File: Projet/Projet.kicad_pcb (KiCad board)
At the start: 4 copper layers, 111 x 81 mm, 67 parts, among them J201 Conn_02x07_Odd_Even, J301 Moteur 1, J302 Moteur 1, J303 Conn_01x03, J401 optiqueGauche, J402 couleursDroit, J403 couleursGauche, J404 optiqueDroit, J405 tofGauche, J406 tofDroit, J501 alim batterie, J502 Conn_01x03_Female, SW201 SW_MEC_5E, U201 STM32G070RBT6, U301 ZXBM5210-S, U302 ZXBM5210-S, U501 AZ1117-5.0, U502 MIC5317-3.3, Y201 16 MHz

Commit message: Routing
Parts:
- removed SW201: SW_MEC_5E, Button_Switch_SMD:SW_SPST_EVQQ2
- added C307: 1uF, Capacitor_SMD:C_0603_1608Metric_Pad1.08x0.95mm_HandSolder, F.Cu at (140.5, 124.2)
- added C308: 1uF, Capacitor_SMD:C_0603_1608Metric_Pad1.08x0.95mm_HandSolder, F.Cu at (181.1, 147.3)
- added C309: 1uF, Capacitor_SMD:C_0603_1608Metric_Pad1.08x0.95mm_HandSolder, F.Cu at (138.1, 140.3)
- added C310: 1uF, Capacitor_SMD:C_0603_1608Metric_Pad1.08x0.95mm_HandSolder, F.Cu at (159.7, 147.5)
- added JP304: SolderJumper_2_Open, Jumper:SolderJumper-2_P1.3mm_Open_TrianglePad1.0x1.5mm, F.Cu at (183.3, 126.1)
- added R401: 2.2k, Resistor_SMD:R_0603_1608Metric_Pad0.98x0.95mm_HandSolder, F.Cu at (176.4, 105.5)
- added R402: 2.2k, Resistor_SMD:R_0603_1608Metric_Pad0.98x0.95mm_HandSolder, F.Cu at (181.0, 105.4)
- added R403: 2.2k, Resistor_SMD:R_0603_1608Metric_Pad0.98x0.95mm_HandSolder, F.Cu at (119.9, 106.9)
- added R404: 2.2k, Resistor_SMD:R_0603_1608Metric_Pad0.98x0.95mm_HandSolder, F.Cu at (123.0, 106.9)
- added S201: 2-1437565-7, 2-1437565-7 (1):SW_2-1437565-7, F.Cu at (197.5, 111.5)
- C305, C306: value 100nF -> 10uF
- C502: value 10uF -> 22uF
- J201: footprint Connector_PinHeader_1.00mm:PinHeader_2x07_P1.00mm_Vertical -> Connector_PinHeader_1.27mm:PinHeader_2x07_P1.27mm_Vertical_SMD
- R201, R202: value 60R -> 1k
- R502: value 100k -> 200k
- R503: value 90k -> 100k
- moved H102 107.7 mm to (100.0, 140.0)
- moved H104 107.7 mm to (200.0, 100.0)
- moved D201 101.8 mm to (200.3, 118.6)
- moved R201 101.6 mm to (200.2, 121.4)
- moved J404 92.8 mm to (109.8, 147.4)
- moved C402 82.1 mm to (115.4, 145.8)
- moved C305 67.7 mm to (126.6, 134.5)
- moved JP302 66.2 mm to (132.3, 136.9), turned to 180 degrees
- moved A601 61.9 mm to (207.6, 105.0), turned to 0 degrees
- moved C303 60.7 mm to (141.1, 140.3)
- moved U301 59.7 mm to (140.0, 132.3), turned to 90 degrees
- moved JP303 59.4 mm to (132.3, 132.7), turned to 180 degrees
- moved J301 56.1 mm to (152.1, 147.4), turned to 180 degrees
- moved J405 53.8 mm to (187.3, 100.4)
- moved JP208 52.0 mm to (146.4, 140.4), turned to -90 degrees
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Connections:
- C201 pad 1: STLINK_NRST -> Net-(C201-Pad1)
- C306 pad 1: V+_batterie -> Net-(C306-Pad1)
- J402 pad 1: +3.3V -> +5V
- JP301 pad 2: +3.3V -> +5V
- JP302 pad 2: +3.3V -> +5V
- U201 pad 12: STLINK_NRST -> Net-(C201-Pad1)
- U201 pad 58: BAT_LED -> unconnected-(U201-Pad58)
- U201 pad 7: unconnected-(U201-Pad7) -> +3.3V
- U302 pad 2: V+_batterie -> Net-(C306-Pad1)
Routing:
- net +5V: track 0.00 -> 165.7 mm, vias 0 -> 6
- net V+_batterie: track 0.00 -> 159.7 mm, vias 0 -> 4
- net /Communication/ESP_EN: track 0.00 -> 91.8 mm, vias 0 -> 2
- net /STM32F070RB/OPTQ1: track 0.00 -> 90.2 mm, vias 0 -> 2
- net /STM32F070RB/OPTQ2: track 0.00 -> 66.6 mm, vias 0 -> 2
- net Net-(A601-Pad14): track 0.00 -> 63.8 mm, vias 0 -> 1
- net Net-(C201-Pad1): track 0.00 -> 62.8 mm, vias 0 -> 2
- net Net-(A601-Pad15): track 0.00 -> 58.8 mm, vias 0 -> 2
- net /Driver_Motor_SERVO/SERV_DATA: track 0.00 -> 51.7 mm, vias 0 -> 2
- net /STM32F070RB/TOF1_GPIO1: track 0.00 -> 49.9 mm
- net Net-(JP208-Pad1): track 0.00 -> 49.8 mm, vias 0 -> 2
- net /STM32F070RB/TOF2_SDA: track 0.00 -> 49.6 mm, vias 0 -> 2
- net /STM32F070RB/TOF1_XSHUT: track 0.00 -> 49.3 mm
- net /STM32F070RB/TOF1_SCL: track 0.00 -> 48.9 mm
- net Net-(JP207-Pad1): track 0.00 -> 47.7 mm, vias 0 -> 2
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- added copper zone on In2.Cu, net +3.3V
- added copper zone on B.Cu, net GND
- added copper zone on F.Cu, net GND
- added copper zone on In1.Cu, net GND
- removed copper zone on B.Cu, net (none)
- removed copper zone on F.Cu, net (none)
- removed copper zone on In1.Cu, net (none)
- removed copper zone on In2.Cu, net (none)
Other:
- board size 111 x 81 mm -> 137.1 x 57 mm

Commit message: PCB_ROUTAGE
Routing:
- net /STM32F070RB/TOF2_XSHUT: track 41.7 -> 38.7 mm
- net /STM32F070RB/TOF2_GPIO1: track 37.7 -> 35.6 mm
- net /STM32F070RB/TOF2_SDA: track 49.6 -> 48.1 mm
- net /STM32F070RB/TOF2_SCL: track 44.4 -> 43.0 mm
- net /STM32F070RB/TOF1_SCL: track 48.9 -> 47.7 mm
- net Net-(JP202-Pad2): track 39.7 -> 40.6 mm
- net Net-(JP204-Pad2): track 22.5 -> 21.6 mm
- net Net-(C304-Pad1): track 40.7 -> 39.9 mm
- net Net-(JP201-Pad2): track 32.8 -> 33.3 mm

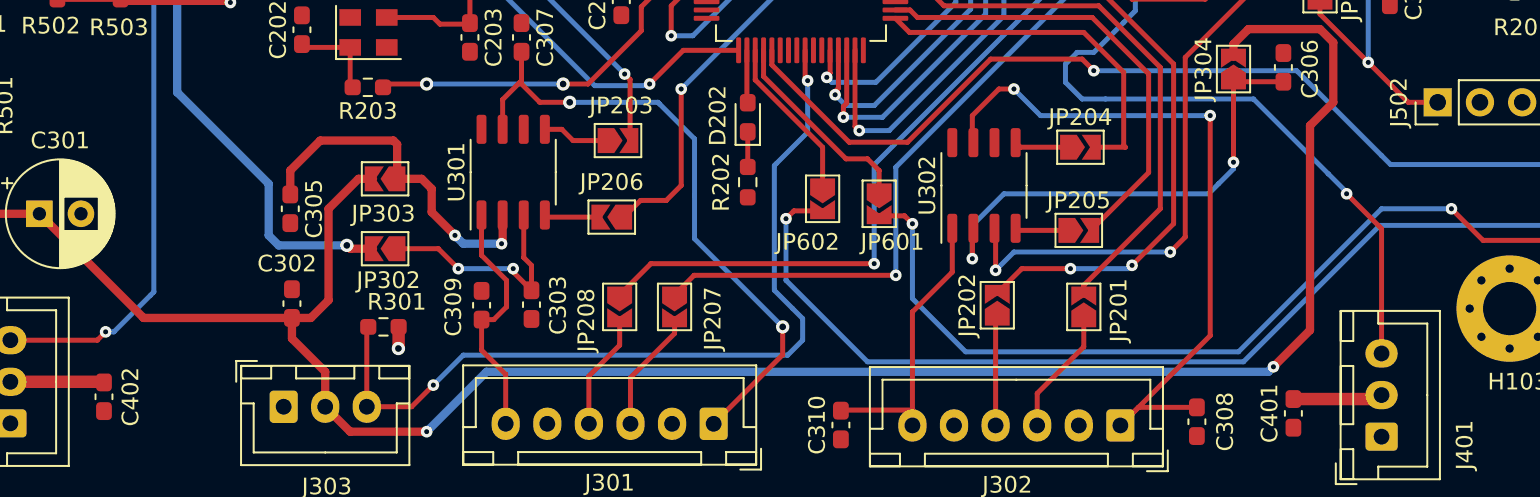
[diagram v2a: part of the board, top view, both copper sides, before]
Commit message: PCB_ROUTAGE_Modif
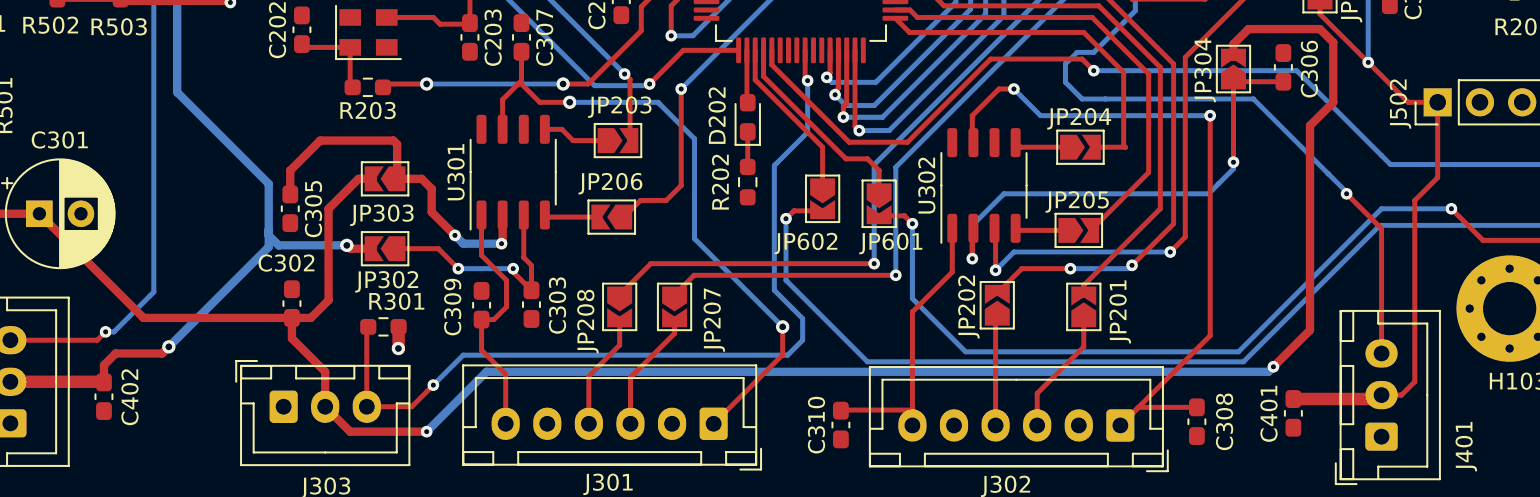
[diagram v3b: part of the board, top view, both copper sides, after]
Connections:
- C401 pad 2: +3.3V -> +5V
- C402 pad 2: +3.3V -> +5V
- J401 pad 2: +3.3V -> +5V
- J404 pad 2: +3.3V -> +5V
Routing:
- net +5V: track 165.7 -> 211.3 mm, vias 6 -> 7
- net +3.3V: track 35.4 -> 24.4 mm
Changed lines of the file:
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@@
       (net 123 "GND") (pintype "passive"))
     (pad "2" smd roundrect (at 0.8625 0 90) (size 1.075 0.95) (layers "F.Cu" "F.Paste" "F.Mask") (roundrect_rratio 0.25)
-      (net 122 "+3.3V") (pintype "passive"))
+      (net 124 "+5V") (pintype "passive"))
     (model "${KICAD6_3DMODEL_DIR}/Capacitor_SMD.3dshapes/C_0603_1608Metric.wrl"
       (offset (xyz 0 0 0))
@@
       (net 123 "GND") (pintype "passive"))
     (pad "2" smd roundrect (at 0.8625 0 90) (size 1.075 0.95) (layers "F.Cu" "F.Paste" "F.Mask") (roundrect_rratio 0.25)
-      (net 122 "+3.3V") (pintype "passive"))
+      (net 124 "+5V") (pintype "passive"))
     (model "${KICAD6_3DMODEL_DIR}/Capacitor_SMD.3dshapes/C_0603_1608Metric.wrl"
       (offset (xyz 0 0 0))
@@
       (net 123 "GND") (pinfunction "Pin_1") (pintype "passive"))
     (pad "2" thru_hole oval (at 2.5 0 90) (size 1.7 1.95) (drill 0.95) (layers *.Cu *.Mask)
-      (net 122 "+3.3V") (pinfunction "Pin_2") (pintype "passive"))
+      (net 124 "+5V") (pinfunction "Pin_2") (pintype "passive"))
     (pad "3" thru_hole oval (at 5 0 90) (size 1.7 1.95) (drill 0.95) (layers *.Cu *.Mask)
       (net 52 "/STM32F070RB/OPTQ2") (pinfunction "Pin_3") (pintype "passive"))
@@
       (net 123 "GND") (pinfunction "Pin_1") (pintype "passive"))
     (pad "2" thru_hole oval (at 2.5 0 90) (size 1.7 1.95) (drill 0.95) (layers *.Cu *.Mask)
-      (net 122 "+3.3V") (pinfunction "Pin_2") (pintype "passive"))
+      (net 124 "+5V") (pinfunction "Pin_2") (pintype "passive"))
     (pad "3" thru_hole oval (at 5 0 90) (size 1.7 1.95) (drill 0.95) (layers *.Cu *.Mask)
       (net 61 "/STM32F070RB/OPTQ1") (pinfunction "Pin_3") (pintype "passive"))
@@
   (segment (start 128.4375 114.55) (end 130.35 114.55) (width 0.5) (layer "F.Cu") (net 122))
   (segment (start 146.5 121.1375) (end 147.8625 121.1375) (width 0.75) (layer "F.Cu") (net 122))
-  (segment (start 115.3625 144.9) (end 115.4 144.9375) (width 0.75) (layer "F.Cu") (net 122))
   (segment (start 119.9 107.825) (end 119.9 109.2125) (width 0.75) (layer "F.Cu") (net 122))
   (segment (start 130.4625 114.5375) (end 130.4 114.6) (width 0.5) (layer "F.Cu") (net 122))
@@
   (segment (start 182 116.84) (end 185.56 116.84) (width 0.5) (layer "F.Cu") (net 122))
   (segment (start 151.625 119.05) (end 151.625 118.55) (width 0.3) (layer "F.Cu") (net 122))
-  (segment (start 191.9625 145.9375) (end 192.2 145.7) (width 0.75) (layer "F.Cu") (net 122))
   (segment (start 176.4 106.4125) (end 176.4 107.7) (width 0.5) (layer "F.Cu") (net 122))
   (segment (start 144.9 115.7) (end 144.9 117.1375) (width 0.75) (layer "F.Cu") (net 122))
@@
   (segment (start 130.35 114.55) (end 130.4 114.6) (width 0.5) (layer "F.Cu") (net 122))
   (segment (start 133.1125 141.6) (end 133.1125 142.8875) (width 0.75) (layer "F.Cu") (net 122))
-  (segment (start 109.775 144.9) (end 115.3625 144.9) (width 0.75) (layer "F.Cu") (net 122))
-  (segment (start 186.9 145.9375) (end 191.9625 145.9375) (width 0.75) (layer "F.Cu") (net 122))
   (segment (start 147.8 115.7) (end 147.8 117.1375) (width 0.75) (layer "F.Cu") (net 122))
   (segment (start 181 106.3125) (end 181 107.6) (width 0.5) (layer "F.Cu") (net 122))
@@
   (segment (start 124.7 112.7) (end 125.5 111.9) (width 0.3) (layer "F.Cu") (net 124))
   (segment (start 119 116.425) (end 122.6375 116.425) (width 0.5) (layer "F.Cu") (net 124))
+  (segment (start 195.575 128.1) (end 195.575 132.625) (width 0.3) (layer "F.Cu") (net 124))
   (segment (start 115.5 115.5) (end 114.75 114.75) (width 0.5) (layer "F.Cu") (net 124))
   (segment (start 119.8 117.225) (end 119 116.425) (width 0.5) (layer "F.Cu") (net 124))
+  (segment (start 119.3 142.8) (end 118.9 143.2) (width 0.5) (layer "F.Cu") (net 124))
   (segment (start 124.7 112.7) (end 114.75 112.7) (width 0.3) (layer "F.Cu") (net 124))
   (segment (start 191.4 125.7) (end 193.8 128.1) (width 0.3) (layer "F.Cu") (net 124))
+  (segment (start 194.2 134) (end 194.2 144.9) (width 0.3) (layer "F.Cu") (net 124))
+  (segment (start 194.2 144.9) (end 193.4 145.7) (width 0.3) (layer "F.Cu") (net 124))
+  (segment (start 115.3625 144.9) (end 115.4 144.9375) (width 0.75) (layer "F.Cu") (net 124))
+  (segment (start 115.4 143.9) (end 115.4 144.9375) (width 0.5) (layer "F.Cu") (net 124))
   (segment (start 193.8 128.1) (end 195.575 128.1) (width 0.3) (layer "F.Cu") (net 124))
+  (segment (start 195.575 132.625) (end 194.2 134) (width 0.3) (layer "F.Cu") (net 124))
   (segment (start 126.1625 114.1625) (end 124.7 112.7) (width 0.3) (layer "F.Cu") (net 124))
   (segment (start 119 116.425) (end 118.075 115.5) (width 0.5) (layer "F.Cu") (net 124))
   (segment (start 134.5 103.2) (end 134.5 99.575) (width 0.3) (layer "F.Cu") (net 124))
+  (segment (start 191.9625 145.9375) (end 192.2 145.7) (width 0.75) (layer "F.Cu") (net 124))
   (segment (start 131.575 136.9) (end 130.2 136.9) (width 0.5) (layer "F.Cu") (net 124))
   (segment (start 188.5 122.8) (end 188.5 122.025) (width 0.3) (layer "F.Cu") (net 124))
   (segment (start 122.6375 116.425) (end 122.7 116.3625) (width 0.5) (layer "F.Cu") (net 124))
+  (segment (start 193.4 145.7) (end 192.2 145.7) (width 0.3) (layer "F.Cu") (net 124))
   (segment (start 132.7 105) (end 134.5 103.2) (width 0.3) (layer "F.Cu") (net 124))
   (segment (start 130.2 136.9) (end 130 136.7) (width 0.5) (layer "F.Cu") (net 124))
   (segment (start 134.5 103.2) (end 135.5 104.2) (width 0.3) (layer "F.Cu") (net 124))
+  (segment (start 118.9 143.2) (end 116.1 143.2) (width 0.5) (layer "F.Cu") (net 124))
+  (segment (start 109.775 144.9) (end 115.3625 144.9) (width 0.75) (layer "F.Cu") (net 124))
   (segment (start 126.1625 114.55) (end 126.1625 114.1625) (width 0.3) (layer "F.Cu") (net 124))
+  (segment (start 186.9 145.9375) (end 191.9625 145.9375) (width 0.75) (layer "F.Cu") (net 124))
+  (segment (start 116.1 143.2) (end 115.4 143.9) (width 0.5) (layer "F.Cu") (net 124))
   (segment (start 114.75 112.7) (end 108.45 112.7) (width 0.5) (layer "F.Cu") (net 124))
   (segment (start 122.7875 116.45) (end 122.7 116.3625) (width 0.5) (layer "F.Cu") (net 124))
@@
   (via (at 138.3 104.2) (size 0.7) (drill 0.3) (layers "F.Cu" "B.Cu") (net 124))
   (via (at 132.7 105) (size 0.8) (drill 0.4) (layers "F.Cu" "B.Cu") (net 124))
+  (via (at 119.3 142.8) (size 0.8) (drill 0.4) (layers "F.Cu" "B.Cu") (net 124))
   (segment (start 186.2 103.7) (end 190.1 107.6) (width 0.3) (layer "B.Cu") (net 124))
   (segment (start 125.3 133) (end 119.8 127.5) (width 0.5) (layer "B.Cu") (net 124))
   (segment (start 152.7 103.7) (end 186.2 103.7) (width 0.3) (layer "B.Cu") (net 124))
   (segment (start 125.9 136.7) (end 125.3 136.1) (width 0.5) (layer "B.Cu") (net 124))
-  (segment (start 125.3 136.1) (end 125.3 133) (width 0.5) (layer "B.Cu") (net 124))
   (segment (start 130 136.7) (end 125.9 136.7) (width 0.5) (layer "B.Cu") (net 124))
   (segment (start 132.4 105) (end 132.7 105) (width 0.3) (layer "B.Cu") (net 124))
+  (segment (start 125.3 136.8) (end 119.3 142.8) (width 0.5) (layer "B.Cu") (net 124))
   (segment (start 190.1 111.8) (end 191.4 113.1) (width 0.3) (layer "B.Cu") (net 124))
+  (segment (start 125.3 135.8) (end 125.3 136.8) (width 0.5) (layer "B.Cu") (net 124))
   (segment (start 125.5 111.9) (end 132.4 105) (width 0.3) (layer "B.Cu") (net 124))
   (segment (start 191.4 113.1) (end 191.4 125.7) (width 0.3) (layer "B.Cu") (net 124))
+  (segment (start 125.3 135.8) (end 125.3 133) (width 0.5) (layer "B.Cu") (net 124))
   (segment (start 119.8 127.5) (end 119.8 118.1) (width 0.5) (layer "B.Cu") (net 124))
   (segment (start 190.1 107.6) (end 190.1 111.8) (width 0.3) (layer "B.Cu") (net 124))
+  (segment (start 125.3 136.1) (end 125.3 135.8) (width 0.5) (layer "B.Cu") (net 124))
   (segment (start 138.3 104.2) (end 152.2 104.2) (width 0.3) (layer "B.Cu") (net 124))
   (segment (start 152.2 104.2) (end 152.7 103.7) (width 0.3) (layer "B.Cu") (net 124))

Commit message: PCB_Modif2
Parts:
- removed U501: AZ1117-5.0, Package_TO_SOT_SMD:SOT-223-3_TabPin2
- removed U502: MIC5317-3.3, Package_TO_SOT_SMD:SOT-23-5
- added IC501: AZ1117CH2-5.0TRG1, AZ1117CH2:SOT230P700X180-4N, F.Cu at (110.9, 113.5)
- added PS501: MIC5317-3.3YM5-TR, MIC5317:SOT95P280X145-5N, F.Cu at (126.9, 115.5)
- S501: value Alimentation -> 100SP1T1B4M2QE
- moved S501 1.68 mm to (99.3, 126.0)
- moved R501 0.71 mm to (108.7, 128.2)
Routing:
- net V+_batterie: track 159.7 -> 168.4 mm
- net +5V: track 211.3 -> 205.1 mm
- net Net-(R501-Pad2): track 7.95 -> 10.1 mm
- net Net-(J501-Pad1): track 7.85 -> 9.72 mm

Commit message: Routage_fini
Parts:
- removed JP201, JP202, JP207, JP208: JP3, Jumper:SolderJumper-2_P1.3mm_Open_TrianglePad1.0x1.5mm
- added JP305: SolderJumper_2_Open, Jumper:SolderJumper-2_P1.3mm_Open_TrianglePad1.0x1.5mm, F.Cu at (146.1, 141.1)
- added JP306: SolderJumper_2_Open, Jumper:SolderJumper-2_P1.3mm_Open_TrianglePad1.0x1.5mm, F.Cu at (153.1, 141.6)
- added JP307: SolderJumper_2_Open, Jumper:SolderJumper-2_P1.3mm_Open_TrianglePad1.0x1.5mm, F.Cu at (177.7, 140.0)
- added JP308: SolderJumper_2_Open, Jumper:SolderJumper-2_P1.3mm_Open_TrianglePad1.0x1.5mm, F.Cu at (164.3, 141.5)
- J301: value Moteur 1 -> Moteur 2
- J402: value couleursDroit -> couleursGauche
- J403: value couleursGauche -> couleursDroit
- J405: value tofGauche -> tofDroit
- J406: value tofDroit -> tofGauche
- moved J502 9.77 mm to (203.3, 122.1), turned to 180 degrees
- moved R501 9.48 mm to (101.7, 134.6)
- moved C201 8.75 mm to (191.1, 115.0)
- moved C308 6.59 mm to (183.5, 141.2)
- moved JP302 6.10 mm to (132.2, 130.8)
- moved C305 5.50 mm to (132.1, 134.4), turned to 180 degrees
- moved C310 5.01 mm to (160.0, 142.5)
- moved R301 4.59 mm to (127.9, 140.0), turned to 90 degrees
- moved JP303 4.30 mm to (132.3, 137.0)
- moved D201 3.33 mm to (197.5, 116.8)
- moved R201 3.33 mm to (197.4, 119.6)
- moved JP304 2.73 mm to (184.6, 128.5), turned to 0 degrees
- moved C303 2.28 mm to (141.4, 138.0), turned to 0 degrees
- moved C306 2.21 mm to (184.2, 125.3), turned to 0 degrees
- moved S201 2.17 mm to (197.6, 109.3)
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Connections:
- net Net-(A601-Pad14) renamed /Communication/ESP_RX_JP
- net Net-(A601-Pad15) renamed /Communication/ESP_TX_JP
- net Net-(C201-Pad1) renamed /STM32F070RB/NRST_sw
- net Net-(C303-Pad1) renamed /Driver_Motor_SERVO/5V_DRV_2
- net Net-(C304-Pad1) renamed /Driver_Motor_SERVO/5V_DRV_1
- net Net-(C305-Pad1) renamed /Driver_Motor_SERVO/VM_DRIVER_2_JP
- net Net-(C306-Pad1) renamed /Driver_Motor_SERVO/VM_DRIVER_1_JP
- net Net-(D201-Pad1) renamed /STM32F070RB/LED_line
- net Net-(J201-Pad13) renamed /STM32F070RB/ST_LINK_TX
- net Net-(J201-Pad14) renamed /STM32F070RB/ST_LINK_RX
- net Net-(JP203-Pad2) renamed /STM32F070RB/DRV_2_REV_JP
- net Net-(JP206-Pad1) renamed /STM32F070RB/DRV_2_FWD_JP
- C307 pad 2: M2- -> /Driver_Motor_SERVO/M2-_JP
- C308 pad 2: M1- -> /Driver_Motor_SERVO/M1-_JP
- C309 pad 2: M2+ -> /Driver_Motor_SERVO/M2+_JP
- C310 pad 2: M1+ -> /Driver_Motor_SERVO/M1+_JP
- J301 pad 5: +3.3V -> +5V
- J302 pad 5: +3.3V -> +5V
- U201 pad 14: unconnected-(U201-Pad14) -> /STM32F070RB/OPTQ1
- U201 pad 24: unconnected-(U201-Pad24) -> /STM32F070RB/OPTQ2
- U201 pad 28: /STM32F070RB/TOF2_GPIO1 -> unconnected-(U201-Pad28)
- U201 pad 29: /STM32F070RB/TOF2_XSHUT -> unconnected-(U201-Pad29)
- U201 pad 36: Net-(JP201-Pad2) -> /Driver_Motor_SERVO/ENC_1_A
- U201 pad 37: Net-(JP202-Pad2) -> /Driver_Motor_SERVO/ENC_1_B
- U201 pad 38: Net-(JP207-Pad1) -> /Driver_Motor_SERVO/ENC_2_A
- U201 pad 39: Net-(JP208-Pad1) -> /Driver_Motor_SERVO/ENC_2_B
- U201 pad 47: /STM32F070RB/OPTQ2 -> /STM32F070RB/TOF2_XSHUT
- U201 pad 48: /STM32F070RB/OPTQ1 -> /STM32F070RB/TOF2_GPIO1
- U301 pad 1: M2+ -> /Driver_Motor_SERVO/M2+_JP
- U301 pad 7: M2- -> /Driver_Motor_SERVO/M2-_JP
- U302 pad 1: M1+ -> /Driver_Motor_SERVO/M1+_JP
- U302 pad 7: M1- -> /Driver_Motor_SERVO/M1-_JP
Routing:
- net +5V: track 205.1 -> 99.6 mm
- net V+_batterie: track 168.4 -> 63.8 mm, vias 4 -> 5
- net Net-(JP208-Pad1): track 50.0 -> 0.00 mm, vias 2 -> 0
- net /Driver_Motor_SERVO/ENC_2_B: track 7.07 -> 56.2 mm, vias 0 -> 2
- net Net-(JP207-Pad1): track 47.7 -> 0.00 mm, vias 2 -> 0
- net /Driver_Motor_SERVO/ENC_2_A: track 7.40 -> 55.0 mm, vias 0 -> 2
- net /Driver_Motor_SERVO/ENC_1_B: track 6.54 -> 48.6 mm, vias 0 -> 2
- net Net-(JP202-Pad2): track 40.6 -> 0.00 mm, vias 2 -> 0
- net M1-: track 43.2 -> 7.72 mm, vias 2 -> 0
- net /Driver_Motor_SERVO/ENC_1_A: track 7.56 -> 42.4 mm
- net /Driver_Motor_SERVO/M1-_JP: track 0.00 -> 33.4 mm, vias 0 -> 2
- net Net-(JP201-Pad2): track 33.3 -> 0.00 mm
- net /Driver_Motor_SERVO/M2-_JP: track 0.00 -> 32.9 mm, vias 0 -> 2
- net M2-: track 38.1 -> 5.96 mm, vias 2 -> 0
- net /STM32F070RB/OPTQ1: track 90.2 -> 61.9 mm
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- added copper zone on In2.Cu, net +5V
- added copper zone on In2.Cu, net V+_batterie
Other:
- board text added: "+"
- board text added: "1"
- board text added: "32"
- board text added: "CARY ESE 2023"
- board text added: "CLR_D"
- board text added: "CLR_G"
- board text added: "GND"
- board text added: "MOTOR_1"
- board text added: "MOTOR_2"
- board text added: "OPT_D"
- board text added: "OPT_G"
- board text added: "SERVO"
- board text added: "TOF_D"
- board text added: "TOF_G"
